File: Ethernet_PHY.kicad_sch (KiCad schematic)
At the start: 16 parts, among them J2 RJ45_Hanrun_HR911105A_Horizon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, U7 LAN8720A, Y1 25MHz

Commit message: Updated footprint
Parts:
- R22, R26, R27, R28, R30: footprint (none) -> Resistor_SMD:R_0603_1608Metric
- Y1: footprint (none) -> Crystal:Crystal_SMD_3225-4Pin_3.2x2.5mm
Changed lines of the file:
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@@
 			)
 		)
-		(property "Footprint" ""
+		(property "Footprint" "Resistor_SMD:R_0603_1608Metric"
 			(at 207.01 93.472 90)
 			(effects
@@
 			)
 		)
-		(property "Footprint" ""
+		(property "Footprint" "Resistor_SMD:R_0603_1608Metric"
 			(at 129.54 107.188 90)
 			(effects
@@
 			)
 		)
-		(property "Footprint" ""
+		(property "Footprint" "Crystal:Crystal_SMD_3225-4Pin_3.2x2.5mm"
 			(at 52.07 115.57 0)
 			(effects
@@
 			)
 		)
-		(property "Footprint" ""
+		(property "Footprint" "Resistor_SMD:R_0603_1608Metric"
 			(at 122.682 118.11 90)
 			(effects
@@
 			)
 		)
-		(property "Footprint" ""
+		(property "Footprint" "Resistor_SMD:R_0603_1608Metric"
 			(at 127.762 118.11 90)
 			(effects
@@
 			)
 		)
-		(property "Footprint" ""
+		(property "Footprint" "Resistor_SMD:R_0603_1608Metric"
 			(at 207.01 83.312 90)
 			(effects

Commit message: Updated Footprint
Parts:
- renumbered C17 to C18, C18 to C19, C11 to C20, C12 to C21, C13 to C22, C14 to C23, C15 to C24, C16 to C25, J2 to J7, R26 to R23, R28 to R24, R27 to R25, R30 to R26, R22 to R27, U7 to U4
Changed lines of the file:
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@@
 		(dnp no)
 		(fields_autoplaced yes)
-		(property "Reference" "#PWR07"
+		(property "Reference" "#PWR046"
 			(at 60.96 67.31 0)
 			(effects
@@
 			(project ""
 				(path "/eefff33b-727a-4f43-882a-17641c879d4f/7eb6205d-ebea-40e3-840d-903808bb0d8c"
-					(reference "#PWR07")
+					(reference "#PWR046")
 					(unit 1)
 				)
@@
 		(on_board yes)
 		(dnp no)
-		(property "Reference" "R22"
+		(property "Reference" "R27"
 			(at 207.01 93.218 0)
 			(effects
@@
 			(project "esp32-based-motherboard"
 				(path "/eefff33b-727a-4f43-882a-17641c879d4f/7eb6205d-ebea-40e3-840d-903808bb0d8c"
-					(reference "R22")
+					(reference "R27")
 					(unit 1)
 				)
@@
 		(on_board yes)
 		(dnp no)
-		(property "Reference" "C13"
+		(property "Reference" "C22"
 			(at 77.216 78.74 0)
 			(effects
@@
 			(project "esp32-based-motherboard"
 				(path "/eefff33b-727a-4f43-882a-17641c879d4f/7eb6205d-ebea-40e3-840d-903808bb0d8c"
-					(reference "C13")
+					(reference "C22")
 					(unit 1)
 				)
@@
 		(dnp no)
 		(fields_autoplaced yes)
-		(property "Reference" "#PWR038"
+		(property "Reference" "#PWR047"
 			(at 60.96 90.17 0)
 			(effects
@@
 			(project ""
 				(path "/eefff33b-727a-4f43-882a-17641c879d4f/7eb6205d-ebea-40e3-840d-903808bb0d8c"
-					(reference "#PWR038")
+					(reference "#PWR047")
 					(unit 1)
 				)
@@
 		(on_board yes)
 		(dnp no)
-		(property "Reference" "R28"
+		(property "Reference" "R24"
 			(at 131.064 103.124 90)
 			(effects
@@
 			(project "esp32-based-motherboard"
 				(path "/eefff33b-727a-4f43-882a-17641c879d4f/7eb6205d-ebea-40e3-840d-903808bb0d8c"
-					(reference "R28")
+					(reference "R24")
 					(unit 1)
 				)
@@
 		(on_board yes)
 		(dnp no)
-		(property "Reference" "C16"
+		(property "Reference" "C25"
 			(at 111.506 58.42 0)
 			(effects
@@
 			(project "esp32-based-motherboard"
 				(path "/eefff33b-727a-4f43-882a-17641c879d4f/7eb6205d-ebea-40e3-840d-903808bb0d8c"
-					(reference "C16")
+					(reference "C25")
 					(unit 1)
 				)
@@
 		(on_board yes)
 		(dnp no)
-		(property "Reference" "C18"
+		(property "Reference" "C19"
 			(at 61.976 127 0)
 			(effects
@@
 			(project "esp32-based-motherboard"
 				(path "/eefff33b-727a-4f43-882a-17641c879d4f/7eb6205d-ebea-40e3-840d-903808bb0d8c"
-					(reference "C18")
+					(reference "C19")
 					(unit 1)
 				)
@@
 		(dnp no)
 		(fields_autoplaced yes)
-		(property "Reference" "#PWR049"
+		(property "Reference" "#PWR053"
 			(at 223.52 95.25 0)
 			(effects
@@
 			(project "esp32-based-motherboard"
 				(path "/eefff33b-727a-4f43-882a-17641c879d4f/7eb6205d-ebea-40e3-840d-903808bb0d8c"
-					(reference "#PWR049")
+					(reference "#PWR053")
 					(unit 1)
 				)
@@
 		(dnp no)
 		(fields_autoplaced yes)
-		(property "Reference" "U7"
+		(property "Reference" "U4"
 			(at 107.5533 130.81 0)
 			(effects
@@
 		)
 		(pin "23"
+		)
+		(instances
+			(project "esp32-based-motherboard"
+				(path "/eefff33b-727a-4f43-882a-17641c879d4f/7eb6205d-ebea-40e3-840d-903808bb0d8c"
+					(reference "U4")
+					(unit 1)
+				)
+			)
 		)
 	)
@@
 		(pin "1"
 		)
+		(instances
+			(project "esp32-based-motherboard"
+				(path "/eefff33b-727a-4f43-882a-17641c879d4f/7eb6205d-ebea-40e3-840d-903808bb0d8c"
+					(reference "Y1")
+					(unit 1)
+				)
+			)
+		)
 	)
 	(symbol
@@
 		(on_board yes)
 		(dnp no)
-		(property "Reference" "C14"
+		(property "Reference" "C23"
 			(at 83.566 78.74 0)
 			(effects
@@
 			(project "esp32-based-motherboard"
 				(path "/eefff33b-727a-4f43-882a-17641c879d4f/7eb6205d-ebea-40e3-840d-903808bb0d8c"
-					(reference "C14")
+					(reference "C23")
 					(unit 1)
 				)
@@
 		(dnp no)
 		(fields_autoplaced yes)
-		(property "Reference" "#FLG04"
+		(property "Reference" "#FLG03"
 			(at 100.965 64.77 0)
 			(effects
@@
 			(project ""
 				(path "/eefff33b-727a-4f43-882a-17641c879d4f/7eb6205d-ebea-40e3-840d-903808bb0d8c"
-					(reference "#FLG04")
+					(reference "#FLG03")
 					(unit 1)
 				)
@@
 		(dnp no)
 		(fields_autoplaced yes)
-		(property "Reference" "#PWR044"
+		(property "Reference" "#PWR051"
 			(at 142.24 105.41 0)
 			(effects
@@
 			(project "esp32-based-motherboard"
 				(path "/eefff33b-727a-4f43-882a-17641c879d4f/7eb6205d-ebea-40e3-840d-903808bb0d8c"
-					(reference "#PWR044")
+					(reference "#PWR051")
 					(unit 1)
 				)
@@
 		(dnp no)
 		(fields_autoplaced yes)
-		(property "Reference" "J2"
+		(property "Reference" "J7"
 			(at 181.61 76.2 0)
 			(effects
@@
 		)
 		(pin "9"
+		)
+		(instances
+			(project "esp32-based-motherboard"
+				(path "/eefff33b-727a-4f43-882a-17641c879d4f/7eb6205d-ebea-40e3-840d-903808bb0d8c"
+					(reference "J7")
+					(unit 1)
+				)
+			)
 		)
 	)
@@
 		(dnp no)
 		(fields_autoplaced yes)
-		(property "Reference" "#PWR042"
+		(property "Reference" "#PWR050"
 			(at 124.46 133.35 0)
 			(effects
@@
 			(project "esp32-based-motherboard"
 				(path "/eefff33b-727a-4f43-882a-17641c879d4f/7eb6205d-ebea-40e3-840d-903808bb0d8c"
-					(reference "#PWR042")
+					(reference "#PWR050")
 					(unit 1)
 				)
@@
 		(dnp no)
 		(fields_autoplaced yes)
-		(property "Reference" "#PWR043"
+		(property "Reference" "#PWR045"
 			(at 52.07 137.16 0)
 			(effects
@@
 			(project "esp32-based-motherboard"
 				(path "/eefff33b-727a-4f43-882a-17641c879d4f/7eb6205d-ebea-40e3-840d-903808bb0d8c"
-					(reference "#PWR043")
+					(reference "#PWR045")
 					(unit 1)
 				)
@@
 		(on_board yes)
 		(dnp no)
-		(property "Reference" "C15"
+		(property "Reference" "C24"
 			(at 105.156 58.42 0)
 			(effects
@@
 			(project "esp32-based-motherboard"
 				(path "/eefff33b-727a-4f43-882a-17641c879d4f/7eb6205d-ebea-40e3-840d-903808bb0d8c"
-					(reference "C15")
+					(reference "C24")
 					(unit 1)
 				)
@@
 		(on_board yes)
 		(dnp no)
-		(property "Reference" "C11"
+		(property "Reference" "C20"
 			(at 62.992 78.486 0)
 			(effects
@@
 			(project "esp32-based-motherboard"
 				(path "/eefff33b-727a-4f43-882a-17641c879d4f/7eb6205d-ebea-40e3-840d-903808bb0d8c"
-					(reference "C11")
+					(reference "C20")
 					(unit 1)
 				)
@@
 		(on_board yes)
 		(dnp no)
-		(property "Reference" "C17"
+		(property "Reference" "C18"
 			(at 46.736 127 0)
 			(effects
@@
 			(project "esp32-based-motherboard"
 				(path "/eefff33b-727a-4f43-882a-17641c879d4f/7eb6205d-ebea-40e3-840d-903808bb0d8c"
-					(reference "C17")
+					(reference "C18")
 					(unit 1)
 				)
@@
 		(on_board yes)
 		(dnp no)
-		(property "Reference" "R26"
+		(property "Reference" "R23"
 			(at 122.428 118.11 0)
 			(effects
@@
 		)
 		(pin "1"
+		)
+		(instances
+			(project "esp32-based-motherboard"
+				(path "/eefff33b-727a-4f43-882a-17641c879d4f/7eb6205d-ebea-40e3-840d-903808bb0d8c"
+					(reference "R23")
+					(unit 1)
+				)
+			)
 		)
 	)
@@
 		(dnp no)
 		(fields_autoplaced yes)
-		(property "Reference" "#PWR048"
+		(property "Reference" "#PWR052"
 			(at 190.5 107.95 0)
 			(effects
@@
 			(project "esp32-based-motherboard"
 				(path "/eefff33b-727a-4f43-882a-17641c879d4f/7eb6205d-ebea-40e3-840d-903808bb0d8c"
-					(reference "#PWR048")
+					(reference "#PWR052")
 					(unit 1)
 				)
@@
 		(on_board yes)
 		(dnp no)
-		(property "Reference" "R27"
+		(property "Reference" "R25"
 			(at 127.508 118.11 0)
 			(effects
@@
 			(project "esp32-based-motherboard"
 				(path "/eefff33b-727a-4f43-882a-17641c879d4f/7eb6205d-ebea-40e3-840d-903808bb0d8c"
-					(reference "R27")
+					(reference "R25")
 					(unit 1)
 				)
@@
 		(on_board yes)
 		(dnp no)
-		(property "Reference" "C12"
+		(property "Reference" "C21"
 			(at 69.596 78.74 0)
 			(effects
@@
 			(project "esp32-based-motherboard"
 				(path "/eefff33b-727a-4f43-882a-17641c879d4f/7eb6205d-ebea-40e3-840d-903808bb0d8c"
-					(reference "C12")
+					(reference "C21")
 					(unit 1)
 				)
@@
 		(on_board yes)
 		(dnp no)
-		(property "Reference" "R30"
+		(property "Reference" "R26"
 			(at 207.01 83.058 0)
 			(effects
@@
 			(project "esp32-based-motherboard"
 				(path "/eefff33b-727a-4f43-882a-17641c879d4f/7eb6205d-ebea-40e3-840d-903808bb0d8c"
-					(reference "R30")
+					(reference "R26")
 					(unit 1)
 				)
@@
 		(dnp no)
 		(fields_autoplaced yes)
-		(property "Reference" "#PWR041"
+		(property "Reference" "#PWR049"
 			(at 105.41 140.97 0)
 			(effects
@@
 			(project "esp32-based-motherboard"
 				(path "/eefff33b-727a-4f43-882a-17641c879d4f/7eb6205d-ebea-40e3-840d-903808bb0d8c"
-					(reference "#PWR041")
+					(reference "#PWR049")
 					(unit 1)
 				)
@@
 		(dnp no)
 		(fields_autoplaced yes)
-		(property "Reference" "#PWR040"
+		(property "Reference" "#PWR048"
 			(at 102.87 43.18 0)
 			(effects
@@
 			(project "esp32-based-motherboard"
 				(path "/eefff33b-727a-4f43-882a-17641c879d4f/7eb6205d-ebea-40e3-840d-903808bb0d8c"
-					(reference "#PWR040")
-					(unit 1)
-				)
+					(reference "#PWR048")
+					(unit 1)
+				)

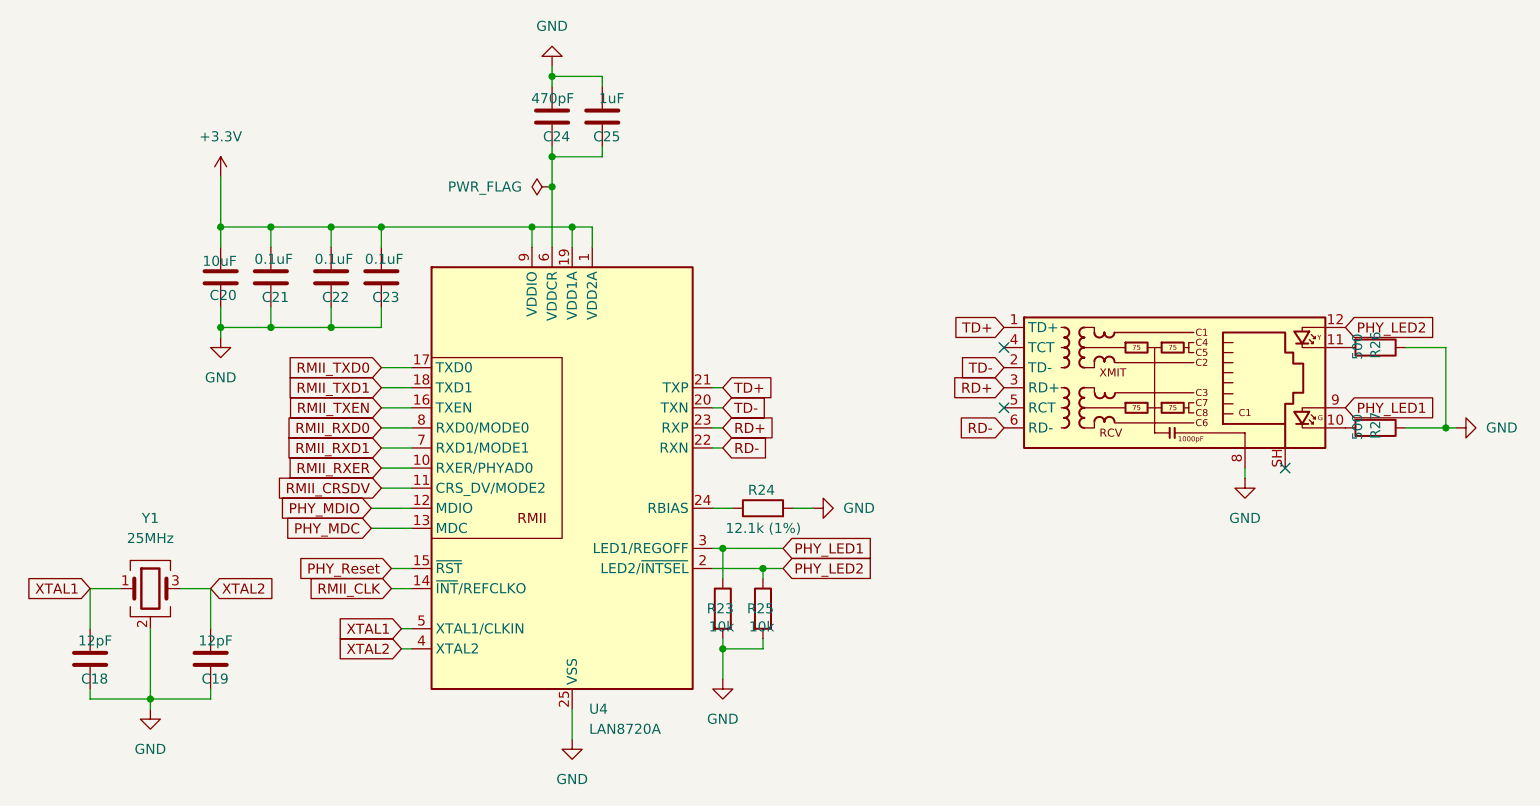
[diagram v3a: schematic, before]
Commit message: Track and Vias added
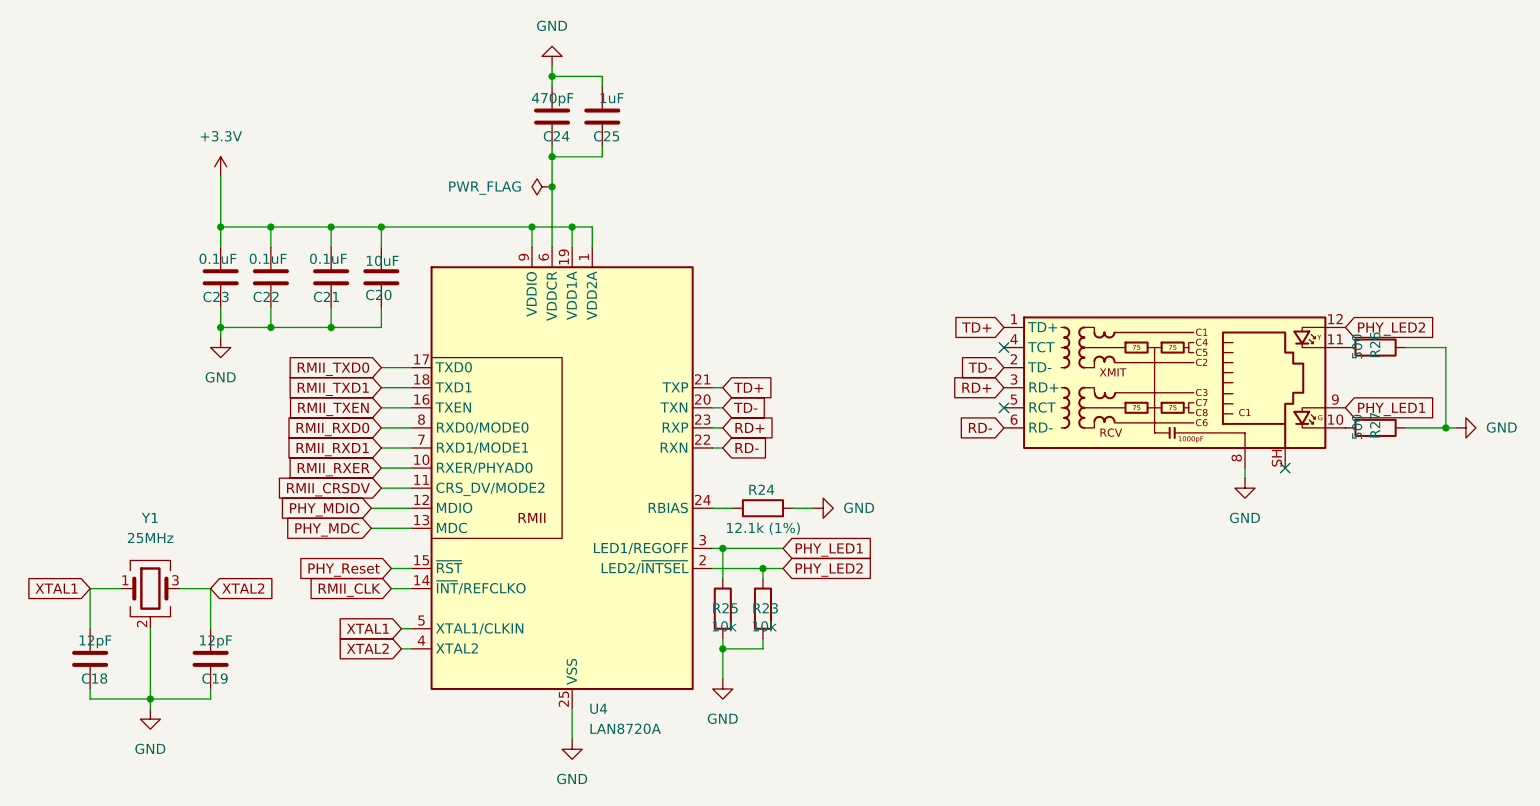
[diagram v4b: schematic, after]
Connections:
- net PHY_LED1: now also R25.1; no longer R23.1
- net PHY_LED2: now also R23.1; no longer R25.1
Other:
- moved on the sheet: C20, C21, C22, C23, R23, R25
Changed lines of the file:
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@@
 	(symbol
 		(lib_id "Device:C")
-		(at 74.93 76.2 180)
+		(at 67.31 76.2 0)
+		(mirror x)
 		(unit 1)
 		(exclude_from_sim no)
@@
 		(dnp no)
 		(property "Reference" "C22"
-			(at 77.216 78.74 0)
+			(at 65.024 78.74 0)
 			(effects
 				(font
@@
 		)
 		(property "Value" "0.1uF"
-			(at 77.724 73.914 0)
+			(at 64.516 73.914 0)
 			(effects
 				(font
@@
 		)
 		(property "Footprint" "Capacitor_SMD:C_0603_1608Metric"
-			(at 73.9648 72.39 0)
+			(at 68.2752 72.39 0)
 			(effects
 				(font
@@
 		)
 		(property "Datasheet" "~"
-			(at 74.93 76.2 0)
+			(at 67.31 76.2 0)
 			(effects
 				(font
@@
 		)
 		(property "Description" "Unpolarized capacitor"
-			(at 74.93 76.2 0)
+			(at 67.31 76.2 0)
 			(effects
 				(font
@@
 	(symbol
 		(lib_id "Device:C")
-		(at 81.28 76.2 180)
+		(at 60.96 76.2 0)
+		(mirror x)
 		(unit 1)
 		(exclude_from_sim no)
@@
 		(dnp no)
 		(property "Reference" "C23"
-			(at 83.566 78.74 0)
+			(at 58.674 78.74 0)
 			(effects
 				(font
@@
 		)
 		(property "Value" "0.1uF"
-			(at 84.074 73.914 0)
+			(at 58.166 73.914 0)
 			(effects
 				(font
@@
 		)
 		(property "Footprint" "Capacitor_SMD:C_0603_1608Metric"
-			(at 80.3148 72.39 0)
+			(at 61.9252 72.39 0)
 			(effects
 				(font
@@
 		)
 		(property "Datasheet" "~"
-			(at 81.28 76.2 0)
+			(at 60.96 76.2 0)
 			(effects
 				(font
@@
 		)
 		(property "Description" "Unpolarized capacitor"
-			(at 81.28 76.2 0)
+			(at 60.96 76.2 0)
 			(effects
 				(font
@@
 	(symbol
 		(lib_id "Device:C")
-		(at 60.96 76.2 180)
+		(at 81.28 76.2 0)
+		(mirror x)
 		(unit 1)
 		(exclude_from_sim no)
@@
 		(dnp no)
 		(property "Reference" "C20"
-			(at 62.992 78.486 0)
+			(at 79.248 78.486 0)
 			(effects
 				(font
@@
 		)
 		(property "Value" "10uF"
-			(at 62.992 74.168 0)
+			(at 79.248 74.168 0)
 			(effects
 				(font
@@
 		)
 		(property "Footprint" "Capacitor_SMD:C_0603_1608Metric"
-			(at 59.9948 72.39 0)
+			(at 82.2452 72.39 0)
 			(effects
 				(font
@@
 		)
 		(property "Datasheet" "~"
-			(at 60.96 76.2 0)
+			(at 81.28 76.2 0)
 			(effects
 				(font
@@
 		)
 		(property "Description" "Unpolarized capacitor"
-			(at 60.96 76.2 0)
+			(at 81.28 76.2 0)
 			(effects
 				(font
@@
 	(symbol
 		(lib_id "Device:R")
-		(at 124.46 118.11 0)
+		(at 129.54 118.11 0)
+		(mirror y)
 		(unit 1)
 		(exclude_from_sim no)
@@
 		(dnp no)
 		(property "Reference" "R23"
-			(at 122.428 118.11 0)
+			(at 131.572 118.11 0)
 			(effects
 				(font
@@
 		)
 		(property "Value" "10k"
-			(at 122.682 120.396 0)
+			(at 131.318 120.396 0)
 			(effects
 				(font
@@
 		)
 		(property "Footprint" "Resistor_SMD:R_0603_1608Metric"
-			(at 122.682 118.11 90)
+			(at 131.318 118.11 90)
 			(effects
 				(font
@@
 		)
 		(property "Datasheet" "~"
-			(at 124.46 118.11 0)
+			(at 129.54 118.11 0)
 			(effects
 				(font
@@
 		)
 		(property "Description" "Resistor"
-			(at 124.46 118.11 0)
+			(at 129.54 118.11 0)
 			(effects
 				(font
@@
 	(symbol
 		(lib_id "Device:R")
-		(at 129.54 118.11 0)
+		(at 124.46 118.11 0)
+		(mirror y)
 		(unit 1)
 		(exclude_from_sim no)
@@
 		(dnp no)
 		(property "Reference" "R25"
-			(at 127.508 118.11 0)
+			(at 126.492 118.11 0)
 			(effects
 				(font
@@
 		)
 		(property "Value" "10k"
-			(at 127.762 120.396 0)
+			(at 126.238 120.396 0)
 			(effects
 				(font
@@
 		)
 		(property "Footprint" "Resistor_SMD:R_0603_1608Metric"
-			(at 127.762 118.11 90)
+			(at 126.238 118.11 90)
 			(effects
 				(font
@@
 		)
 		(property "Datasheet" "~"
-			(at 129.54 118.11 0)
+			(at 124.46 118.11 0)
 			(effects
 				(font
@@
 		)
 		(property "Description" "Resistor"
-			(at 129.54 118.11 0)
+			(at 124.46 118.11 0)
 			(effects
 				(font
@@
 	(symbol
 		(lib_id "Device:C")
-		(at 67.31 76.2 180)
+		(at 74.93 76.2 0)
+		(mirror x)
 		(unit 1)
 		(exclude_from_sim no)
@@
 		(dnp no)
 		(property "Reference" "C21"
-			(at 69.596 78.74 0)
+			(at 72.644 78.74 0)
 			(effects
 				(font
@@
 		)
 		(property "Value" "0.1uF"
-			(at 70.104 73.914 0)
+			(at 72.136 73.914 0)
 			(effects
 				(font
@@
 		)
 		(property "Footprint" "Capacitor_SMD:C_0603_1608Metric"
-			(at 66.3448 72.39 0)
+			(at 75.8952 72.39 0)
 			(effects
 				(font
@@
 		)
 		(property "Datasheet" "~"
-			(at 67.31 76.2 0)
+			(at 74.93 76.2 0)
 			(effects
 				(font
@@
 		)
 		(property "Description" "Unpolarized capacitor"
-			(at 67.31 76.2 0)
-			(effects
-				(font
+			(at 74.93 76.2 0)
+			(effects
+				(font

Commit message: Updated
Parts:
- added C36, C37, C38, C39: 12pF, Capacitor_SMD:C_0603_1608Metric, symbol Device:C
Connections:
- net GND: now also C36.1, C37.1, C38.1, C39.1
- net RD+ renamed ETH_RD+
- net ETH_RD+: now also C39.2
- net RD- renamed ETH_RD-
- net ETH_RD-: now also C38.2
- net RMII_CRSDV: no longer names the net of U4.11 (CRS_DV/MODE2)
- net TD+ renamed ETH_TD+
- net ETH_TD+: now also C36.2
- net TD- renamed ETH_TD-
- net ETH_TD-: now also C37.2
